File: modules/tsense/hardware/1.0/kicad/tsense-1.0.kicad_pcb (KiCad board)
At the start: 2 copper layers, 75 x 75 mm, 29 parts, among them J1 T0, J2 RET, J3 DEP, J4 RTG, J5 DPG, J6 OVL, J7 OVL, J8 OVL, J9 CAN, SW1 CONFIG, SW2 SW_DIP_x08, U7 Teensy_3.2, U8 MCP2551-I-P, U9 TMR1-1211

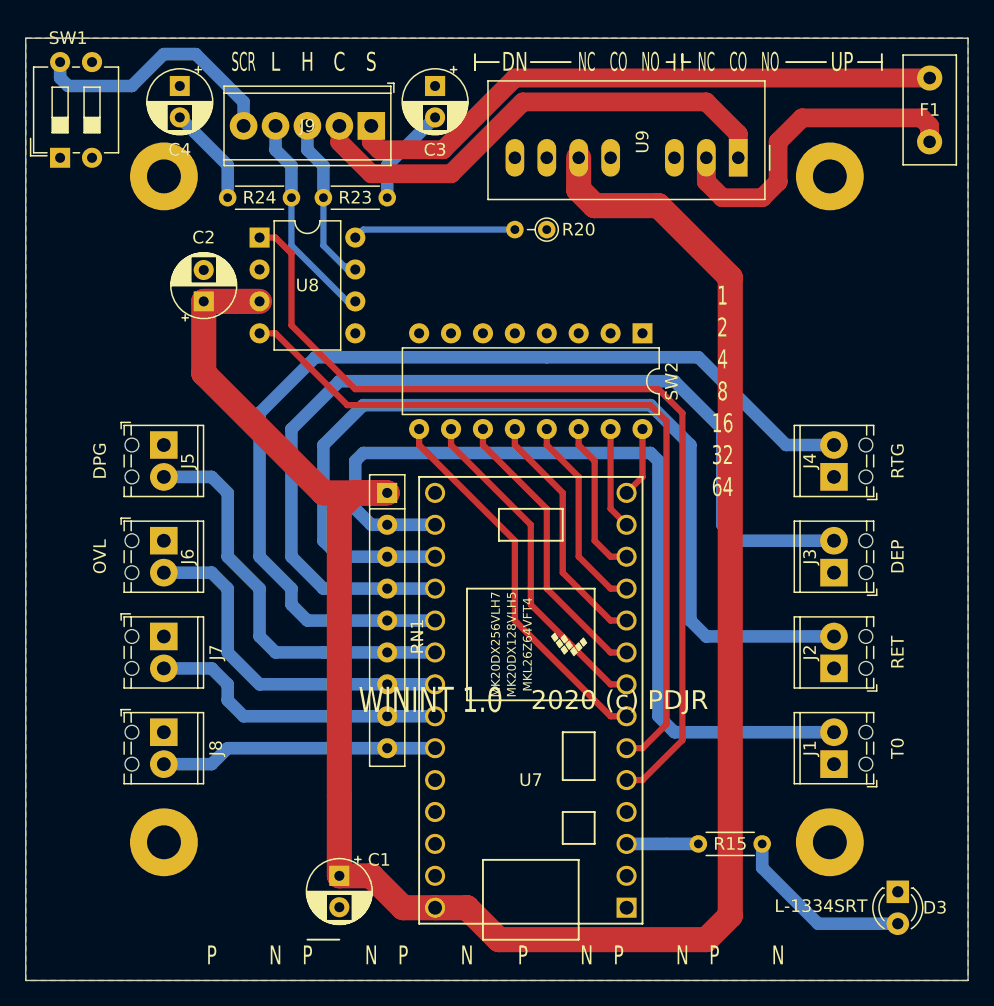
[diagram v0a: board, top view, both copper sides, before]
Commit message: New tsense module
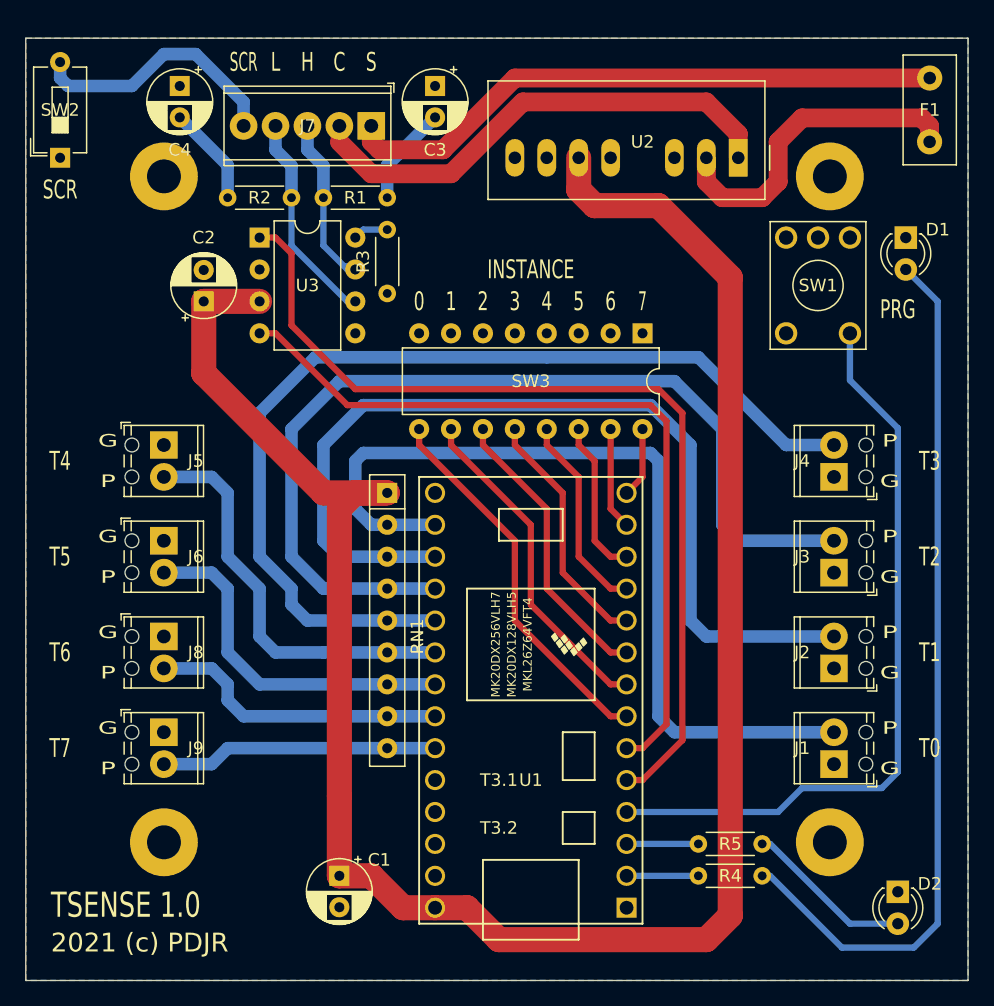
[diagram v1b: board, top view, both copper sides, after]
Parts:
- added D1: L-1334SRT, LED_THT:LED_D3.0mm_FlatTop, F.Cu at (206.0, 102.9)
- added R4: 200R, Resistor_THT:R_Axial_DIN0204_L3.6mm_D1.6mm_P5.08mm_Horizontal, F.Cu at (189.5, 153.7)
- added SW2: SCR, Button_Switch_THT:SW_DIP_SPSTx01_Slide_6.7x4.1mm_W7.62mm_P2.54mm_LowProfile, F.Cu at (138.7, 96.5)
- D2: renamed from D3; footprint LED_THT:LED_D3.0mm -> LED_THT:LED_D3.0mm_FlatTop
- J2: value RET -> T1
- J3: value DEP -> T2
- J4: value RTG -> T3
- J5: value DPG -> T4
- J6: value OVL -> T5
- J8: renamed from J7; value OVL -> T6
- J9: renamed from J8; value OVL -> T7
- R3: renamed from R20; footprint Resistor_THT:R_Axial_DIN0204_L3.6mm_D1.6mm_P2.54mm_Vertical -> Resistor_THT:R_Axial_DIN0204_L3.6mm_D1.6mm_P5.08mm_Horizontal
- SW1: value CONFIG -> PRG; footprint Button_Switch_THT:SW_DIP_SPSTx02_Slide_6.7x6.64mm_W7.62mm_P2.54mm_LowProfile -> Button_Switch_THT:KSA_Tactile_SPST
- SW3: renamed from SW2; value SW_DIP_x08 -> INSTANCE
- moved SW1 64.4 mm to (201.6, 110.5), turned to 180 degrees
- moved R3 13.7 mm to (164.8, 107.3), turned to 90 degrees
- renumbered J9 to J7, R23 to R1, R24 to R2, R15 to R5, U7 to U1, U9 to U2, U8 to U3
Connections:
- SW1 pad 1: GND -> Net-(SW1-Pad1)
- SW1 pad 4: /CAN_SCR -> (no net)
- U1 pad 2: (no net) -> /LED_PRG
- U1 pad 4: (no net) -> Net-(SW1-Pad1)
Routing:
- net Net-(D1-Pad2): track 0.00 -> 70.2 mm
- net Net-(SW1-Pad1): track 0.00 -> 59.4 mm
- net Net-(R3-Pad2): track 13.0 -> 2.80 mm
- net /LED_PRG: track 0.00 -> 5.72 mm
- net Net-(D2-Pad2): track 14.5 -> 13.4 mm
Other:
- board text added: "0"
- board text added: "2021 (c) PDJR"
- board text added: "3"
- board text added: "5"
- board text added: "6"
- board text added: "7"
- board text added: "G P"
- board text added: "P G"
- board text added: "TSENSE 1.0"
- board text removed: "16"
- board text removed: "2020 (c) PDJR"
- board text removed: "32"
- board text removed: "64"
- board text removed: "8"
- board text removed: "CO"
- board text removed: "DN"
- board text removed: "N"
- board text removed: "NC"
- board text removed: "NO"
- board text removed: "P"
- board text removed: "WININT 1.0"

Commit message: Finalise PCB
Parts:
- added D3: L-1334SRT, LED_THT:LED_D3.0mm_FlatTop, F.Cu at (206.0, 108.0)
- added R6: 200R, Resistor_THT:R_Axial_DIN0204_L3.6mm_D1.6mm_P5.08mm_Horizontal, F.Cu at (189.5, 151.1)
- moved R5 26.2 mm to (163.5, 148.6), turned to 180 degrees
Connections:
- U1 pad 25: (no net) -> /LED_PWR
- U1 pad 3: /LED_PWR -> /LED_ERR
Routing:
- net Net-(D3-Pad2): track 0.00 -> 55.5 mm
- net Net-(D2-Pad2): track 13.4 -> 60.0 mm
- net Net-(D1-Pad2): track 70.2 -> 62.4 mm
- net /LED_ERR: track 0.00 -> 5.72 mm
- net /LED_PWR: track 5.72 -> 5.08 mm

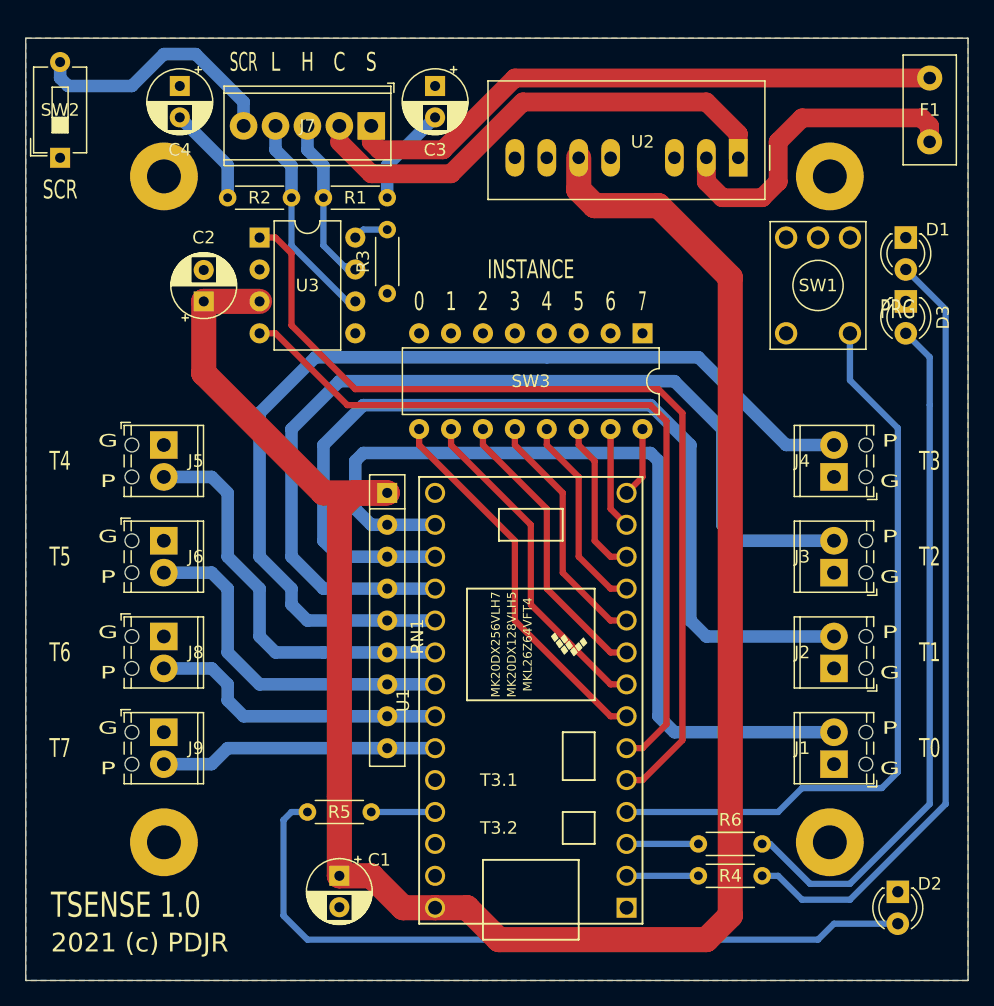
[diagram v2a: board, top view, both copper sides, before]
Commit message: Add programme function
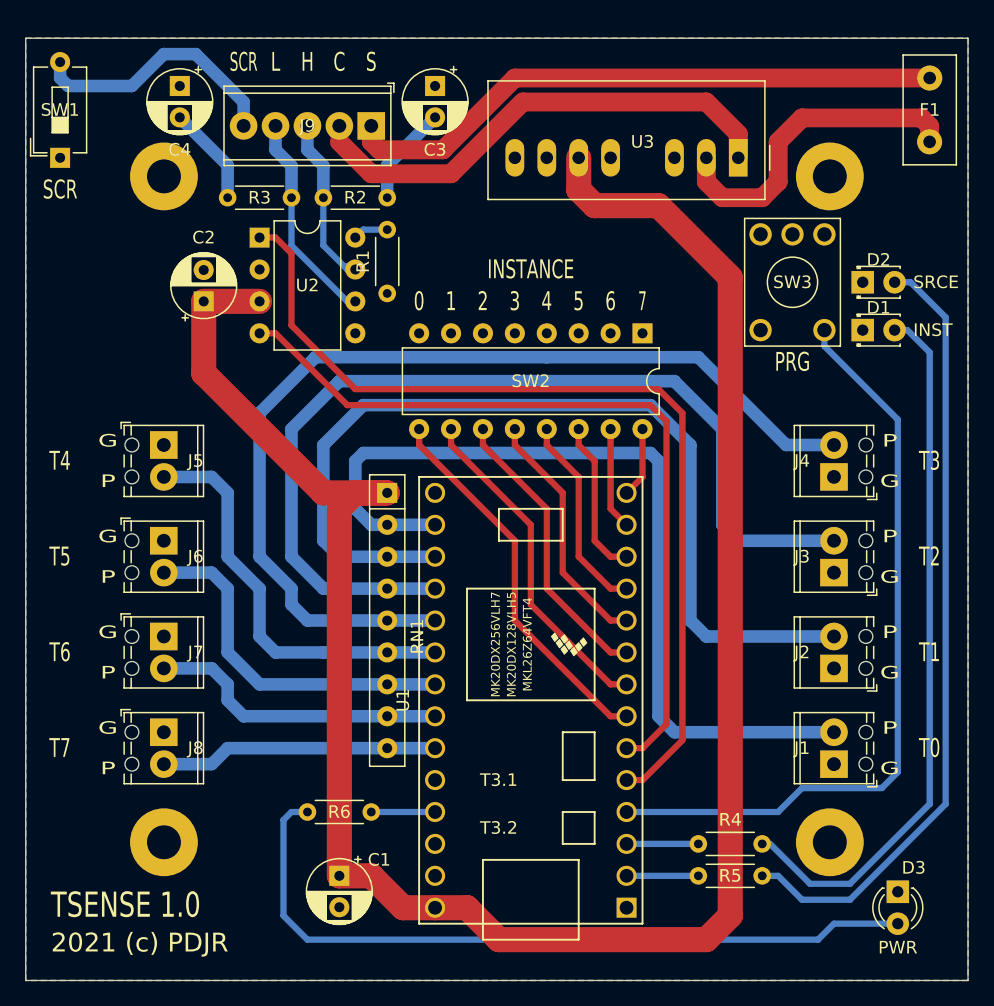
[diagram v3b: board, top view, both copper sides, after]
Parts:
- removed the D3 at (206.0, 108.0)
- removed the SW1 at (201.6, 110.5)
- added D1: INST, LED_THT:LED_D1.8mm_W3.3mm_H2.4mm, F.Cu at (202.6, 110.2)
- added SW3: PRG, Button_Switch_THT:KSA_Tactile_SPST, F.Cu at (199.6, 110.2)
- D2: renamed from D1; value L-1334SRT -> SRCE; footprint LED_THT:LED_D3.0mm_FlatTop -> LED_THT:LED_D1.8mm_W3.3mm_H2.4mm
- D3: renamed from D2; value L-1334SRT -> PWR
- moved D2 4.94 mm to (202.6, 106.4), turned to 0 degrees
- renumbered J8 to J7, J9 to J8, J7 to J9, R3 to R1, R1 to R2, R2 to R3, R6 to R4, R4 to R5, R5 to R6, SW2 to SW1, SW3 to SW2, U3 to U2, U2 to U3
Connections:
- net /LED_ERR renamed /LED_PRG1
- net /LED_PRG renamed /LED_PRG2
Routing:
- net Net-(D1-Pad2): track 55.5 -> 56.8 mm
- net Net-(SW3-Pad1): track 59.4 -> 60.5 mm
- net Net-(D2-Pad2): track 62.4 -> 63.3 mm

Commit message: Codeing
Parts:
- added D3: SRCE, LED_THT:LED_D1.8mm_W3.3mm_H2.4mm, F.Cu at (202.6, 102.6)
- added R6: 200R, Resistor_THT:R_Axial_DIN0204_L3.6mm_D1.6mm_P5.08mm_Horizontal, F.Cu at (189.5, 153.7)
- D1: value INST -> SENS
- D2: value SRCE -> INST
- moved R4 2.54 mm to (189.5, 148.6)
- moved R5 2.54 mm to (189.5, 151.1)
- renumbered D3 to D4, R6 to R7
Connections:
- R4 pad 1: /LED_PRG1 -> /LED_SENSOR
- R5 pad 1: /LED_PRG2 -> /LED_INSTANCE
- SW3 pad 1: Net-(SW3-Pad1) -> GND
- SW3 pad 2: GND -> Net-(SW3-Pad2)
- U1 pad 2: /LED_PRG2 -> /LED_SOURCE
- U1 pad 24: (no net) -> Net-(SW3-Pad2)
- U1 pad 3: /LED_PRG1 -> /LED_INSTANCE
- U1 pad 4: Net-(SW3-Pad1) -> /LED_SENSOR
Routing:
- net Net-(SW3-Pad2): track 0.00 -> 156.0 mm
- net Net-(D3-Pad2): track 0.00 -> 66.1 mm
- net Net-(SW3-Pad1): track 60.5 -> 0.00 mm
- net Net-(D1-Pad2): track 56.8 -> 51.0 mm
- net /LED_SOURCE: track 0.00 -> 5.72 mm
- net /LED_SENSOR: track 0.00 -> 5.72 mm
- net /LED_PRG2: track 5.72 -> 0.00 mm
- net /LED_PRG1: track 5.72 -> 0.00 mm
- net /LED_INSTANCE: track 0.00 -> 5.72 mm
- net Net-(D2-Pad2): track 63.3 -> 61.4 mm
